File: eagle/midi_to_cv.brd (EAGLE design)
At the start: 100.3 x 80 mm, 45 parts, among them IC2 4504N, IC3 4099N, U1 ATMEGA328P_PDIP

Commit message: wider traces and starting distro board
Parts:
- R22: value 2k4 -> 1k
- R6: value 270 -> 470
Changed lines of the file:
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@@
 <?xml version="1.0" encoding="utf-8"?>
 <!DOCTYPE eagle SYSTEM "eagle.dtd">
-<eagle version="7.2.0">
+<eagle version="7.1.0">
 <drawing>
 <settings>
@@
 <element name="R4" library="rcl" package="0207/10" value="4.7k" x="40.64" y="39.37" rot="R90"/>
 <element name="R5" library="rcl" package="0207/10" value="220" x="11.43" y="69.215"/>
-<element name="R6" library="rcl" package="0207/10" value="270" x="26.035" y="66.04" rot="R90"/>
+<element name="R6" library="rcl" package="0207/10" value="470" x="26.035" y="66.04" rot="R90"/>
 <element name="U$11" library="Texas Instruments_By_element14_Batch_1" package="DIP16" value="TLV5628C/I" x="30.48" y="13.97" rot="R270"/>
 <element name="U$4" library="adafruit" package="FB" value="FB" x="80.645" y="67.31" rot="R180"/>
@@
 <element name="JP2" library="pinhead" package="1X08" value="" x="59.69" y="19.05" rot="R180"/>
 <element name="JP3" library="pinhead" package="1X08" value="" x="83.185" y="19.05" rot="R180"/>
-<element name="R22" library="rcl" package="0207/10" value="2k4" x="22.225" y="62.865" rot="R90"/>
+<element name="R22" library="rcl" package="0207/10" value="1k" x="22.225" y="62.865" rot="R90"/>
 <element name="LED" library="con-molex" package="22-23-2021" value="22-23-2021" x="45.72" y="44.45" rot="R270">
 <attribute name="OC_NEWARK" value="25C3832" x="45.72" y="44.45" size="1.778" layer="27" rot="R270" display="off"/>

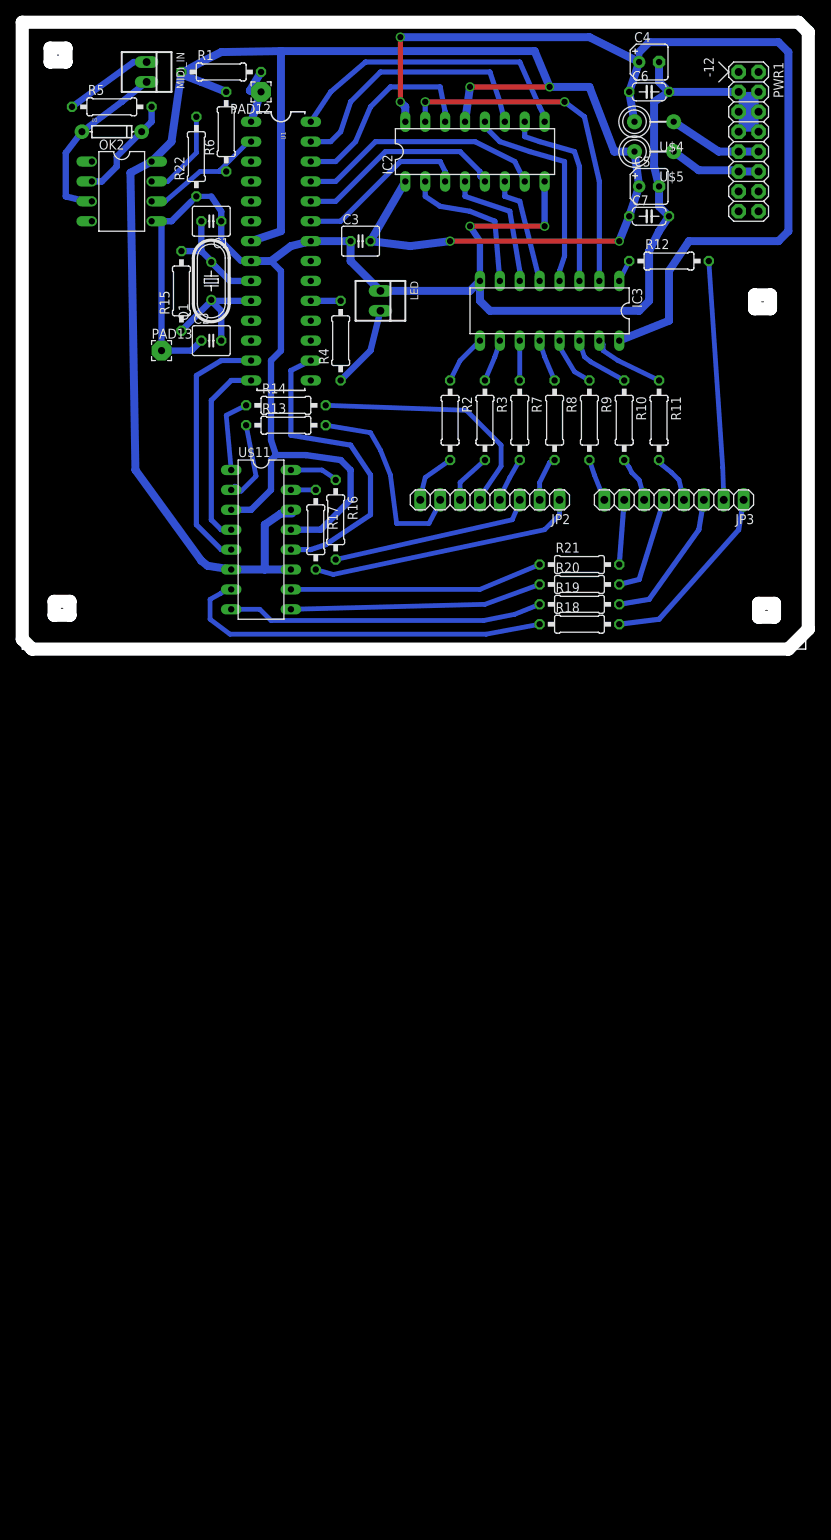
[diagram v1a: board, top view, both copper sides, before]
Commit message: adding opamps
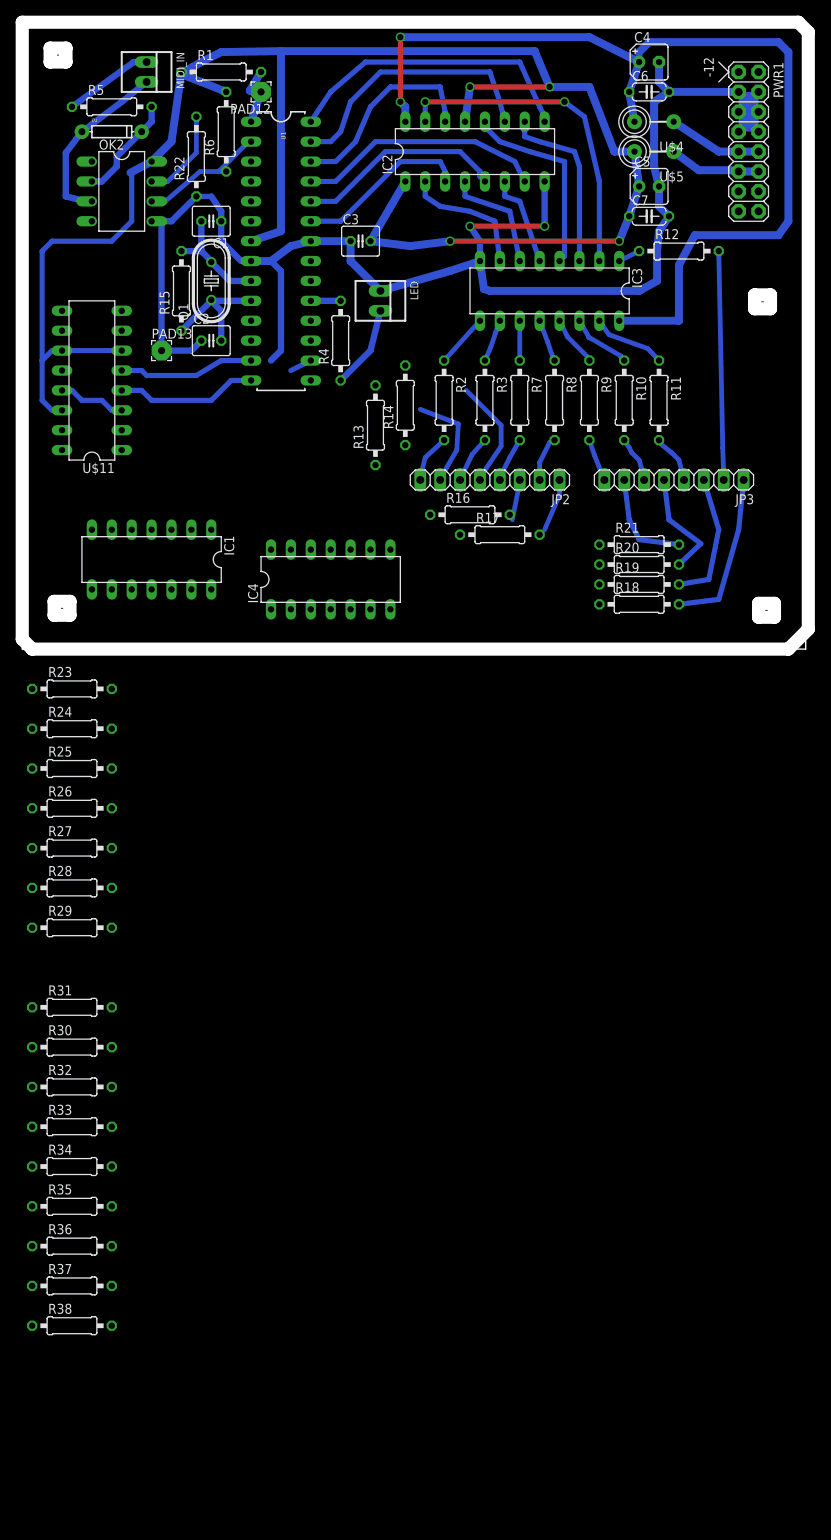
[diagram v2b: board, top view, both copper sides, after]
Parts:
- added IC1, IC4: TL074P, linear:DIL14
- added R23, R24, R25, R26, R27, R28, R29, R31: 1k, rcl:0207/10
- added R30, R32, R33, R34, R35, R36, R37, R38: 1k8, rcl:0207/10
- moved U$11 29.6 mm to (8.89, 34.3), turned to 90 degrees
- moved R17 23.5 mm to (61.0, 14.6), turned to 0 degrees
- moved R16 17.2 mm to (57.1, 17.1), turned to 0 degrees
- moved R14 15.2 mm to (48.9, 31.1), turned to 90 degrees
- moved R13 11.4 mm to (45.1, 28.6), turned to 90 degrees
- moved R18 8.03 mm to (78.7, 5.71)
- moved R19 8.03 mm to (78.7, 8.26)
- moved R20 8.03 mm to (78.7, 10.8)
- moved R21 8.03 mm to (78.7, 13.3)
- moved R2 2.65 mm to (53.8, 31.8)
- moved IC3 2.54 mm to (67.3, 45.7)
- moved JP2 2.54 mm to (59.7, 21.6)
- moved JP3 2.54 mm to (83.2, 21.6)
- moved R10 2.54 mm to (76.8, 31.8)
- moved R11 2.54 mm to (81.3, 31.8)
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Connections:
- new net N$26: IC4.14, R21.1
- new net N$42: IC4.8, R20.1
- new net N$43: IC4.7, R19.1
- new net N$63: IC1.5, R25.2
- new net N$64: IC1.12, R26.2
- new net N$65: IC4.5, R28.2
- new net N$66: IC4.10, R29.2
- new net N$67: R23.1, U$11.2
- new net N$68: IC4.12, R31.2
- new net N$69: R25.1, U$11.1
- new net N$70: R24.1, U$11.16
- new net N$71: R26.1, U$11.15
- new net V+: IC1.4, IC4.4
- new net V-: IC1.11, IC4.11
- net N$52: now also IC4.1, R18.1; no longer R13.1, U$11.2
- net N$53: now also IC1.14, R17.1; no longer R14.1, U$11.1
- net N$54: now also IC1.8; no longer U$11.16
- net N$55: now also IC1.1, R13.1; no longer R17.1, U$11.15
- net N$56: now also IC1.7, R14.1; no longer R18.1, U$11.7
- net N$57: now also IC1.3, R23.2; no longer R19.1, U$11.8
- net N$58: now also IC1.10, R24.2; no longer R20.1, U$11.9
- net N$59: now also IC4.3, R27.2; no longer R21.1, U$11.10
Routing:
- net N$56: track 48.5 -> 0.00 mm
- net GND: track 226.4 -> 184.5 mm
- net N$57: track 40.3 -> 0.00 mm
- net N$15: track 39.9 -> 2.84 mm
- net N$59: track 32.4 -> 0.00 mm
- net N$58: track 32.2 -> 0.00 mm
- net N$29: track 34.5 -> 6.74 mm
- net +5V: track 258.0 -> 235.9 mm
- net N$28: track 25.8 -> 5.17 mm
- net N$24: track 32.1 -> 14.1 mm
- net N$14: track 32.3 -> 17.3 mm
- net N$22: track 25.5 -> 13.7 mm
- net N$52: track 11.0 -> 0.00 mm
- net N$53: track 9.85 -> 0.00 mm
- net N$54: track 6.42 -> 0.00 mm
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
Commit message: feedbacks in place
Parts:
- removed R13, R14, R16, R17, R18, R19, R20, R21: 1k, rcl:0207/10
- added C10, C11, C8, C9: 100n, rcl:C050-024X044
- R30, R32, R33, R34, R35, R36, R37, R38: device rcl:0207/10 -> rcl:0204V
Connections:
- removed net N$40: JP3.1, R18.2
- removed net N$42: IC4.8, R20.1
- removed net V+: IC1.4, IC4.4
- removed net V-: IC1.11, IC4.11
- net +12V: now also C10.1, C8.1, IC1.4, IC4.4
- net GND: now also C11.2, C9.2, IC1.11, IC4.11, R23.1, R24.1, R25.1, R26.1, R27.1, R28.1, R29.1, R31.1
- net N$22: now also IC1.1, R30.2; no longer R13.2
- net N$24: now also C8.2, C9.1; no longer JP2.5, R14.2
- net N$26: now also C10.2, C11.1; no longer IC4.14, R21.1
- net N$28: now also IC1.8, R33.2; no longer R16.2
- net N$29: now also IC1.14, R34.2; no longer R17.2
- net N$34: now also IC4.8, R37.2; no longer R20.2
- net N$41: now also IC4.7, R36.2; no longer R19.2
- net N$43: now also IC4.12, U$11.10; no longer IC4.7, R19.1
- net N$51: now also IC4.14, R38.2; no longer R21.2
- net N$52: now also JP3.1, R35.2; no longer R18.1
- net N$53: now also IC4.10, U$11.9; no longer IC1.14, R17.1
- net N$54: now also IC4.5, U$11.8; no longer IC1.8, R16.1
- net N$55: now also IC4.3, U$11.7; no longer IC1.1, R13.1
- net N$56: now also JP2.5, R32.2; no longer R14.1
- net N$57: now also IC1.2, R30.1; no longer IC1.3
- net N$58: now also IC1.9, R33.1; no longer IC1.10
- net N$59: now also IC1.6, R25.2, R32.1; no longer IC4.3, R27.2
- net N$63: now also IC1.13, R26.2, R34.1; no longer IC1.5, R25.2
- net N$64: now also IC4.2, R27.2, R35.1; no longer IC1.12, R26.2
- net N$65: now also IC4.6, R36.1; no longer IC4.5
- net N$66: now also IC4.9, R37.1; no longer IC4.10
- net N$67: now also IC4.13, R31.2, R38.1; no longer R23.1, U$11.2
- net N$68: now also IC1.12, U$11.15; no longer IC4.12, R31.2
- net N$69: now also IC1.10, U$11.16; no longer R25.1, U$11.1
- net N$70: now also IC1.5, U$11.1; no longer R24.1, U$11.16
- net N$71: now also IC1.3, U$11.2; no longer R26.1, U$11.15
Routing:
- net N$40: track 20.7 -> 0.00 mm
- net N$24: track 14.1 -> 0.00 mm
- net N$51: track 13.1 -> 7.96 mm
- net N$34: track 14.1 -> 10.2 mm
- net N$41: track 17.0 -> 13.1 mm

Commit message: started routing
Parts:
- removed C10, C8: 100n, rcl:C050-024X044
- moved C11 146.6 mm to (72.4, 19.1), turned to 180 degrees
- moved C9 122.7 mm to (17.8, 24.1), turned to 270 degrees
- moved R38 117.6 mm to (78.7, 6.35)
- moved R35 115.6 mm to (78.7, 19.1)
- moved R36 112.4 mm to (66.0, 19.1), turned to 180 degrees
- moved R37 106.0 mm to (66.0, 6.35), turned to 180 degrees
- moved R34 97.1 mm to (16.5, 30.5), turned to 90 degrees
- moved R31 88.8 mm to (80.0, 3.81), turned to 180 degrees
- moved R27 86.3 mm to (83.8, 12.7), turned to 90 degrees
- moved R30 81.3 mm to (3.81, 30.5), turned to 90 degrees
- moved R33 79.4 mm to (16.5, 17.8), turned to 270 degrees
- moved R32 73.7 mm to (3.81, 17.8), turned to 270 degrees
- moved R29 71.5 mm to (66.0, 3.81), turned to 180 degrees
- moved R28 70.4 mm to (61.0, 14.0), turned to 90 degrees
- moved R26 55.0 mm to (12.7, 34.3)
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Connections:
- removed net N$24: C8.2, C9.1
- removed net N$26: C10.2, C11.1
- net +12V: now also C11.1, C9.1; no longer C10.1, C8.1
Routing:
- net +5V: track 235.9 -> 180.8 mm
- net N$27: track 18.1 -> 0.00 mm
- net N$14: track 17.3 -> 0.00 mm
- net N$22: track 13.7 -> 0.00 mm
- net N$41: track 13.1 -> 0.00 mm
- net N$34: track 10.2 -> 0.00 mm
- net GND: track 184.5 -> 175.9 mm
- net N$51: track 7.96 -> 0.00 mm
- net N$29: track 6.74 -> 0.00 mm
- net N$28: track 5.17 -> 0.00 mm
- net N$15: track 2.84 -> 0.00 mm
- net N$21: track 29.2 -> 26.7 mm
- net N$3: track 6.22 -> 3.89 mm
- net N$8: track 5.77 -> 3.65 mm
- net N$7: track 5.72 -> 3.70 mm
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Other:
- outline, holes or cut-outs redrawn

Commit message: opamps
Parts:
- moved R24 6.35 mm to (19.1, 14.0), turned to 180 degrees
- moved R26 3.05 mm to (15.7, 34.3)
- moved R25 1.27 mm to (10.2, 11.4)
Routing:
- net N$22: track 0.00 -> 97.2 mm
- net N$29: track 0.00 -> 86.3 mm
- net N$56: track 0.00 -> 84.0 mm
- net N$28: track 0.00 -> 66.1 mm
- net GND: track 175.9 -> 202.5 mm
- net N$57: track 0.00 -> 11.8 mm
- net N$63: track 0.00 -> 2.54 mm
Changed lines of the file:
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@@
 <element name="IC4" library="linear" package="DIL14" value="TL074P" x="72.39" y="12.7" rot="R180"/>
 <element name="R23" library="rcl" package="0207/10" value="1k" x="8.89" y="36.83" rot="R180"/>
-<element name="R24" library="rcl" package="0207/10" value="1k" x="12.7" y="13.97"/>
-<element name="R25" library="rcl" package="0207/10" value="1k" x="8.89" y="11.43" rot="R180"/>
-<element name="R26" library="rcl" package="0207/10" value="1k" x="12.7" y="34.29"/>
+<element name="R24" library="rcl" package="0207/10" value="1k" x="19.05" y="13.97" rot="R180"/>
+<element name="R25" library="rcl" package="0207/10" value="1k" x="10.16" y="11.43" rot="R180"/>
+<element name="R26" library="rcl" package="0207/10" value="1k" x="15.748" y="34.29"/>
 <element name="R27" library="rcl" package="0207/10" value="1k" x="83.82" y="12.7" rot="R90"/>
 <element name="R28" library="rcl" package="0207/10" value="1k" x="60.96" y="13.97" rot="R90"/>
@@
 <contactref element="IC1" pad="1"/>
 <contactref element="R30" pad="2"/>
-<wire x1="6.35" y1="31.75" x2="55.118" y2="24.13" width="0" layer="19" extent="1-1"/>
-<wire x1="3.81" y1="31.75" x2="6.35" y2="31.75" width="0" layer="19" extent="1-1"/>
+<wire x1="6.35" y1="31.75" x2="7.62" y2="31.75" width="0.8128" layer="16"/>
+<wire x1="7.62" y1="31.75" x2="8.636" y2="30.48" width="0.8128" layer="16"/>
+<wire x1="8.636" y1="30.48" x2="8.636" y2="8.636" width="0.8128" layer="16"/>
+<wire x1="8.636" y1="8.636" x2="11.43" y2="3.81" width="0.8128" layer="16"/>
+<wire x1="11.43" y1="3.81" x2="54.61" y2="3.81" width="0.8128" layer="16"/>
+<wire x1="54.61" y1="3.81" x2="55.88" y2="5.08" width="0.8128" layer="16"/>
+<wire x1="55.88" y1="5.08" x2="55.88" y2="21.59" width="0.8128" layer="16"/>
+<wire x1="55.88" y1="21.59" x2="55.118" y2="22.352" width="0.8128" layer="16"/>
+<wire x1="55.118" y1="22.352" x2="55.118" y2="24.13" width="0.8128" layer="16"/>
+<wire x1="3.81" y1="31.75" x2="6.35" y2="31.75" width="0.8128" layer="16"/>
 </signal>
 <signal name="N$28">
@@
 <contactref element="R33" pad="2"/>
 <contactref element="IC1" pad="8"/>
-<wire x1="16.51" y1="16.51" x2="65.278" y2="24.13" width="0" layer="19" extent="1-1"/>
 <wire x1="13.97" y1="16.51" x2="16.51" y2="16.51" width="0" layer="19" extent="1-1"/>
+<wire x1="16.51" y1="16.51" x2="45.72" y2="16.51" width="0.8128" layer="16"/>
+<wire x1="45.72" y1="16.51" x2="49.53" y2="20.32" width="0.8128" layer="16"/>
+<wire x1="49.53" y1="20.32" x2="49.53" y2="29.21" width="0.8128" layer="16"/>
+<wire x1="49.53" y1="29.21" x2="52.07" y2="31.75" width="0.8128" layer="16"/>
+<wire x1="52.07" y1="31.75" x2="62.23" y2="31.75" width="0.8128" layer="16"/>
+<wire x1="62.23" y1="31.75" x2="65.278" y2="28.702" width="0.8128" layer="16"/>
+<wire x1="65.278" y1="28.702" x2="65.278" y2="24.13" width="0.8128" layer="16"/>
 </signal>
 <signal name="N$29">
@@
 <contactref element="IC1" pad="14"/>
 <contactref element="R34" pad="2"/>
-<wire x1="16.51" y1="31.75" x2="70.358" y2="24.13" width="0" layer="19" extent="1-1"/>
-<wire x1="13.97" y1="31.75" x2="16.51" y2="31.75" width="0" layer="19" extent="1-1"/>
+<wire x1="70.358" y1="24.13" x2="70.358" y2="25.908" width="0.8128" layer="16"/>
+<wire x1="70.358" y1="25.908" x2="69.596" y2="26.67" width="0.8128" layer="16"/>
+<wire x1="69.596" y1="26.67" x2="69.596" y2="31.496" width="0.8128" layer="16"/>
+<wire x1="69.596" y1="31.496" x2="67.31" y2="33.782" width="0.8128" layer="16"/>
+<wire x1="67.31" y1="33.782" x2="51.816" y2="33.782" width="0.8128" layer="16"/>
+<wire x1="51.816" y1="33.782" x2="48.006" y2="29.972" width="0.8128" layer="16"/>
+<wire x1="48.006" y1="29.972" x2="48.006" y2="21.082" width="0.8128" layer="16"/>
+<wire x1="48.006" y1="21.082" x2="44.958" y2="18.034" width="0.8128" layer="16"/>
+<wire x1="44.958" y1="18.034" x2="24.638" y2="18.034" width="0.8128" layer="16"/>
+<wire x1="24.638" y1="18.034" x2="21.59" y2="21.082" width="0.8128" layer="16"/>
+<wire x1="21.59" y1="21.082" x2="21.59" y2="28.956" width="0.8128" layer="16"/>
+<wire x1="21.59" y1="28.956" x2="18.796" y2="31.75" width="0.8128" layer="16"/>
+<wire x1="18.796" y1="31.75" x2="16.51" y2="31.75" width="0.8128" layer="16"/>
+<wire x1="16.51" y1="31.75" x2="13.97" y2="31.75" width="0.8128" layer="16"/>
 </signal>
 <signal name="N$41">
@@
 <wire x1="91.44" y1="66.04" x2="91.44" y2="68.58" width="0" layer="19" extent="1-1"/>
 <wire x1="91.44" y1="71.12" x2="93.98" y2="71.12" width="0" layer="19" extent="1-1"/>
-<wire x1="13.97" y1="36.83" x2="17.78" y2="38.1" width="0" layer="19" extent="1-1"/>
 <wire x1="34.29" y1="30.48" x2="31.75" y2="36.83" width="0" layer="19" extent="16-16"/>
-<wire x1="7.62" y1="34.29" x2="13.97" y2="36.83" width="0" layer="19" extent="1-1"/>
 <wire x1="31.75" y1="22.86" x2="34.29" y2="30.48" width="0" layer="19" extent="1-1"/>
-<wire x1="13.97" y1="24.13" x2="7.62" y2="34.29" width="0" layer="19" extent="1-1"/>
-<wire x1="17.78" y1="21.59" x2="13.97" y2="24.13" width="0" layer="19" extent="1-1"/>
-<wire x1="13.97" y1="11.43" x2="17.78" y2="21.59" width="0" layer="19" extent="1-1"/>
-<wire x1="7.62" y1="13.97" x2="13.97" y2="11.43" width="0" layer="19" extent="1-1"/>
+<wire x1="15.24" y1="11.43" x2="17.78" y2="21.59" width="0" layer="19" extent="1-1"/>
+<wire x1="24.13" y1="13.97" x2="15.24" y2="11.43" width="0" layer="19" extent="1-1"/>
 <wire x1="69.85" y1="19.05" x2="78.74" y2="45.72" width="0" layer="19" extent="16-16"/>
 <wire x1="72.39" y1="8.89" x2="69.85" y2="19.05" width="0" layer="19" extent="1-1"/>
@@
 <wire x1="83.82" y1="7.62" x2="72.39" y2="8.89" width="0" layer="19" extent="1-1"/>
 <wire x1="85.09" y1="3.81" x2="83.82" y2="7.62" width="0" layer="19" extent="1-1"/>
+<wire x1="10.668" y1="34.29" x2="10.16" y2="34.036" width="0.8128" layer="16"/>
+<wire x1="10.16" y1="34.036" x2="10.16" y2="25.654" width="0.8128" layer="16"/>
+<wire x1="10.16" y1="25.654" x2="12.192" y2="24.13" width="0.8128" layer="16"/>
+<wire x1="12.192" y1="24.13" x2="13.97" y2="24.13" width="0.8128" layer="16"/>
+<wire x1="13.97" y1="24.13" x2="15.24" y2="24.13" width="0.8128" layer="16"/>
+<wire x1="15.24" y1="24.13" x2="17.78" y2="21.59" width="0.8128" layer="16"/>
+<wire x1="10.668" y1="34.29" x2="12.7" y2="35.56" width="0.8128" layer="16"/>
+<wire x1="12.7" y1="35.56" x2="13.97" y2="36.83" width="0.8128" layer="16"/>
+<wire x1="13.97" y1="36.83" x2="16.51" y2="36.83" width="0.8128" layer="16"/>
+<wire x1="16.51" y1="36.83" x2="17.78" y2="38.1" width="0.8128" layer="16"/>
 </signal>
 <signal name="N$52">
@@
 <contactref element="R32" pad="2"/>
 <contactref element="JP2" pad="5"/>
-<wire x1="6.35" y1="16.51" x2="60.198" y2="24.13" width="0" layer="19" extent="1-1"/>
 <wire x1="3.81" y1="16.51" x2="6.35" y2="16.51" width="0" layer="19" extent="1-1"/>
+<wire x1="6.35" y1="16.51" x2="6.35" y2="13.97" width="0.8128" layer="16"/>
+<wire x1="6.35" y1="13.97" x2="7.112" y2="12.7" width="0.8128" layer="16"/>
+<wire x1="7.112" y1="12.7" x2="7.112" y2="8.382" width="0.8128" layer="16"/>
+<wire x1="7.112" y1="8.382" x2="10.16" y2="2.54" width="0.8128" layer="16"/>
+<wire x1="10.16" y1="2.54" x2="55.88" y2="2.54" width="0.8128" layer="16"/>
+<wire x1="55.88" y1="2.54" x2="58.42" y2="5.08" width="0.8128" layer="16"/>
+<wire x1="58.42" y1="5.08" x2="58.42" y2="19.05" width="0.8128" layer="16"/>
+<wire x1="58.42" y1="19.05" x2="59.69" y2="20.32" width="0.8128" layer="16"/>
+<wire x1="59.69" y1="20.32" x2="59.69" y2="23.622" width="0.8128" layer="16"/>
+<wire x1="59.69" y1="23.622" x2="60.198" y2="24.13" width="0.8128" layer="16"/>
 </signal>
 <signal name="N$57">
@@
 <contactref element="R23" pad="2"/>
 <contactref element="R30" pad="1"/>
-<wire x1="3.81" y1="29.21" x2="3.81" y2="36.83" width="0" layer="19" extent="1-1"/>
-<wire x1="6.35" y1="29.21" x2="3.81" y2="29.21" width="0" layer="19" extent="1-1"/>
+<wire x1="6.35" y1="29.21" x2="3.81" y2="29.21" width="0.8128" layer="16"/>
+<wire x1="3.81" y1="36.83" x2="3.81" y2="35.56" width="0.8128" layer="16"/>
+<wire x1="3.81" y1="35.56" x2="1.778" y2="33.528" width="0.8128" layer="16"/>
+<wire x1="1.778" y1="33.528" x2="1.778" y2="31.242" width="0.8128" layer="16"/>
+<wire x1="1.778" y1="31.242" x2="3.81" y2="29.21" width="0.8128" layer="16"/>
 </signal>
 <signal name="N$58">
@@
 <contactref element="R33" pad="1"/>
 <wire x1="13.97" y1="19.05" x2="16.51" y2="19.05" width="0" layer="19" extent="1-1"/>
-<wire x1="17.78" y1="13.97" x2="16.51" y2="19.05" width="0" layer="19" extent="1-1"/>
+<wire x1="13.97" y1="13.97" x2="16.51" y2="19.05" width="0" layer="19" extent="1-1"/>
 </signal>
 <signal name="N$59">
@@
 <contactref element="R32" pad="1"/>
 <wire x1="3.81" y1="19.05" x2="6.35" y2="19.05" width="0" layer="19" extent="1-1"/>
-<wire x1="3.81" y1="11.43" x2="3.81" y2="19.05" width="0" layer="19" extent="1-1"/>
+<wire x1="5.08" y1="11.43" x2="3.81" y2="19.05" width="0" layer="19" extent="1-1"/>
 </signal>
 <signal name="N$63">
@@
 <contactref element="R26" pad="2"/>
 <contactref element="R34" pad="1"/>
-<wire x1="16.51" y1="29.21" x2="17.78" y2="34.29" width="0" layer="19" extent="1-1"/>
-<wire x1="13.97" y1="29.21" x2="16.51" y2="29.21" width="0" layer="19" extent="1-1"/>
+<wire x1="16.51" y1="29.21" x2="20.828" y2="34.29" width="0" layer="19" extent="1-1"/>
+<wire x1="16.51" y1="29.21" x2="13.97" y2="29.21" width="0.8128" layer="16"/>
 </signal>
 <signal name="N$64">
